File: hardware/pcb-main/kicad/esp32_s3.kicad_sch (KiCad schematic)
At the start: 14 parts, among them SW2 RESET, SW3 BOOT, U3 ESP32-S3-WROOM-1-N16R8

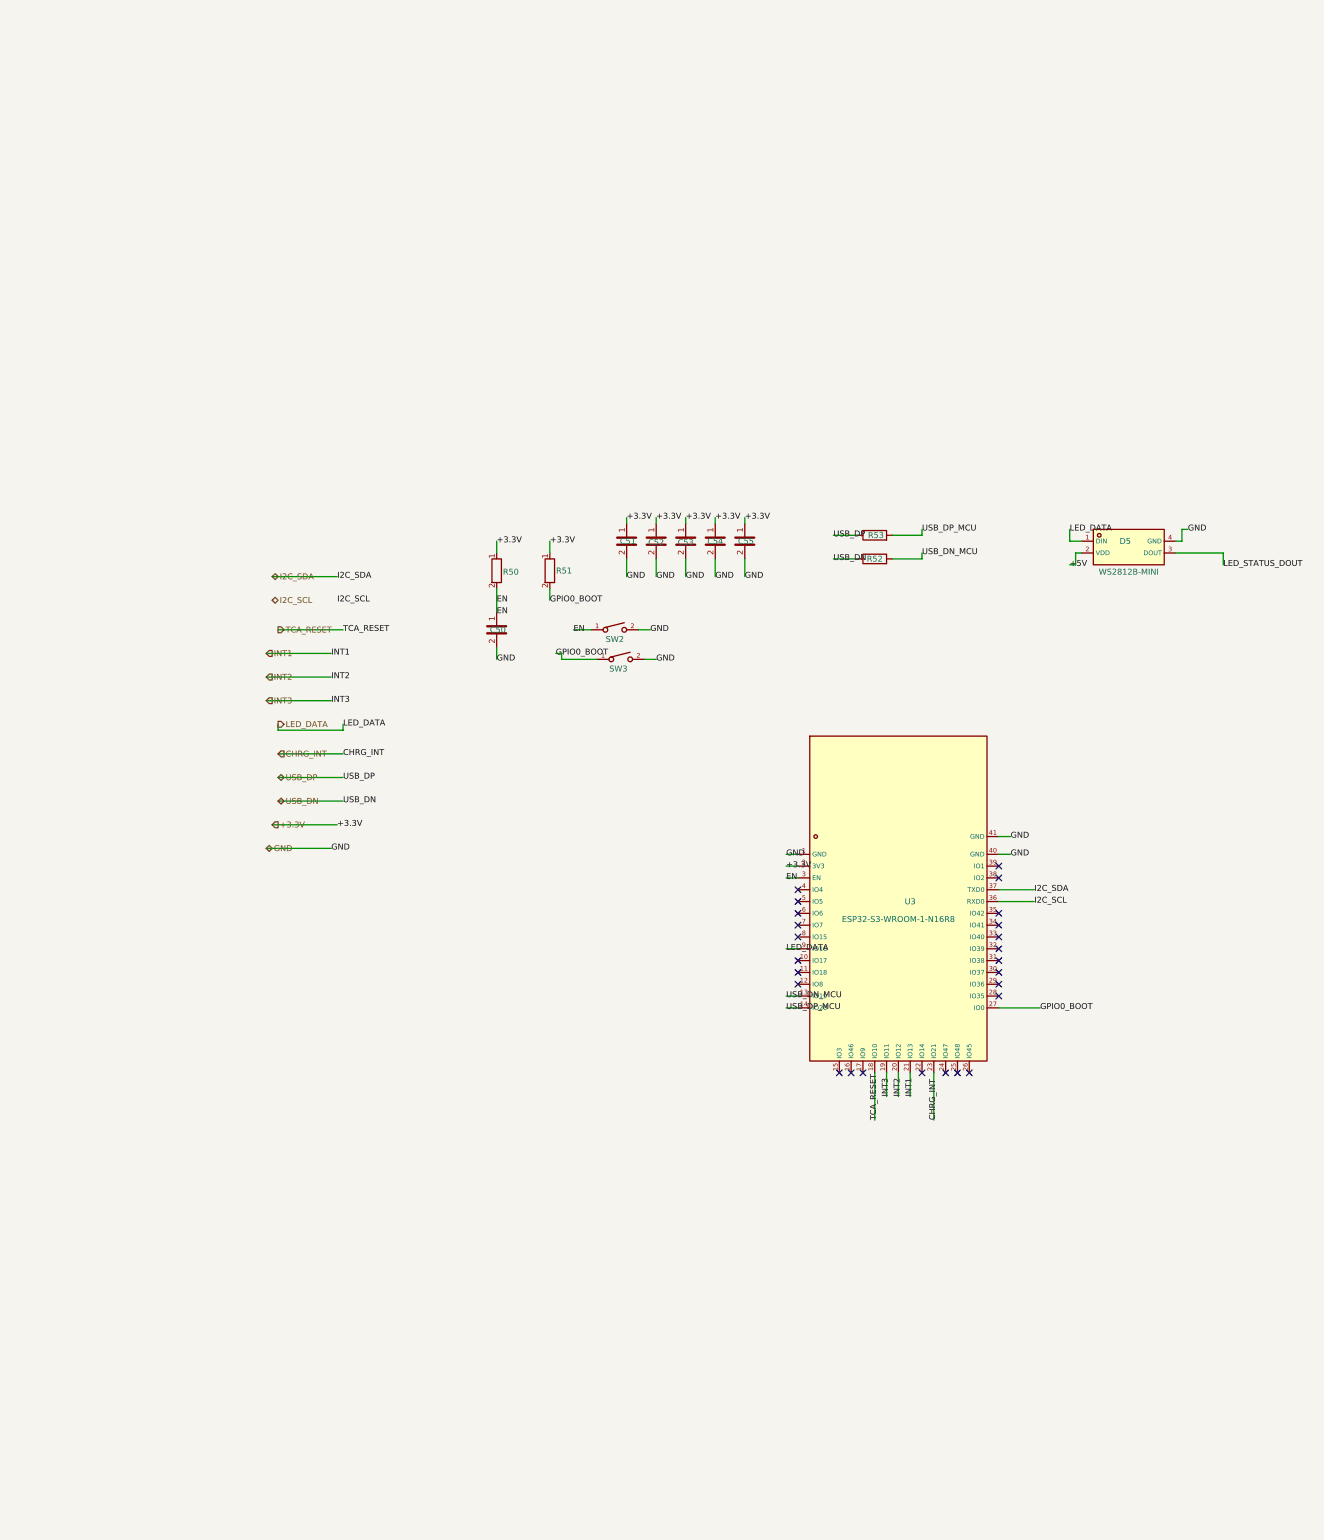
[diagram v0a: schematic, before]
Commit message: Fix Phase 1d schematic issues: SW1, USB pins, +5V, +3.3V direction
- Fix SW1 power switch: pin 3 was wired to VSYS (same as pin 1),
  making the switch always-on. Changed to no-connect so the SPDT
  switch can actually disconnect VSYS from the boost input.
- Add USB_DP/USB_DN sheet pins to power_management reference on root
  so USB data signals can flow between power and root sheets.
- Add +5V hierarchical label to ESP32_S3 sheet and matching sheet pin
  on root, connecting status LED D5 to the global +5V rail.
- Change +3.3V hlabel/pin direction from input to output on power
  management sheet since AMS1117 now produces +3.3V there.
- Add reusable helpers to modify.py: find_sheet_ref, add_pin_to_sheet_ref,
  change_hlabel_shape, change_sheet_pin_direction, label/wire surgery.

Made-with: Cursor
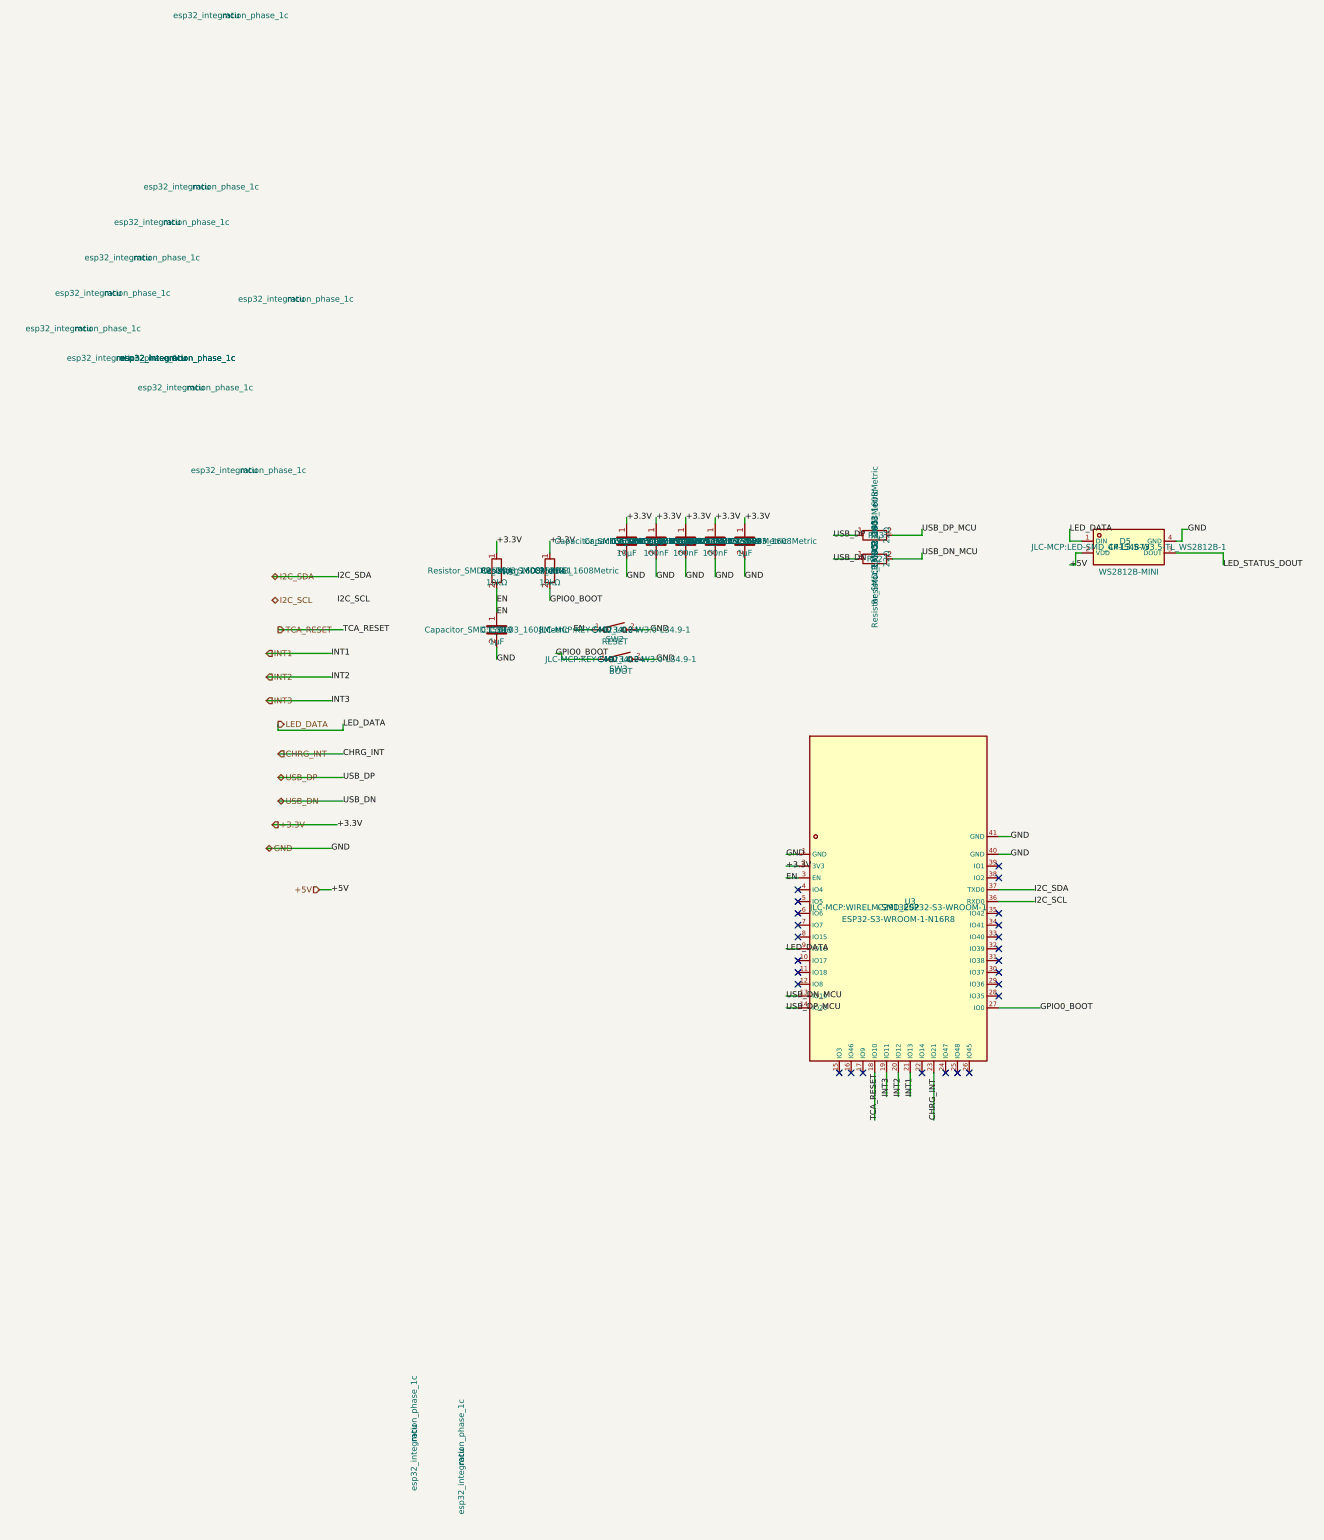
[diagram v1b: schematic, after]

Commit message: Complete Phase 1d/1e: manual wiring, ERC clean (0 errors)
Root sheet:
- Wire ESP32_S3 sheet pins to system nets via labels (I2C_SDA,
  I2C_SCL, TCA_RESET, LED_DATA, CHRG_INT, USB_DP, USB_DN)
- Connect power pins with +3.3V, +5V, GND power symbols
- Add PWR_FLAG symbols to resolve power-not-driven ERC errors
- NC flags on INT1/2/3 (design decision to drop interrupt lines)
- Remove TPIO11/12/13 (INT test points, no longer needed)
- Clean up dangling wires from old U2/U1 area
- Remove stray I2C_SCL hierarchical label

Power management sheet:
- Wire J7 D+/D- pads (A6/B6 tied to USB_DP, A7/B7 tied to USB_DN)
- Insert VSYS_SW into power path: R44 and INA219 IN+ now on
  VSYS_SW net so SW1 actually disconnects boost converter input
- Position AMS1117, caps, USBLC6, power switch components

ESP32_S3 sheet:
- Add no-connect on D5 DOUT (status LED has no downstream chain)
- Component positioning cleanup

ERC: 0 errors, 69 warnings (all benign JLC-MCP pin type mismatches
and footprint library path issues)

Made-with: Cursor
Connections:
- net LED_STATUS_DOUT: no longer names the net of D5.3 (DOUT)
- no-connect marks 25 -> 26
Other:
- moved on the sheet: C50, C51, C52, C53, C54, C55, D5, R50, R51, R52, R53, SW2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
